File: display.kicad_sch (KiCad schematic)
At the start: 16 parts, among them J10 HDMI-A_WE_685119134923, J9 JST_SM_1x10_SM10B-SURS-TF-LF-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

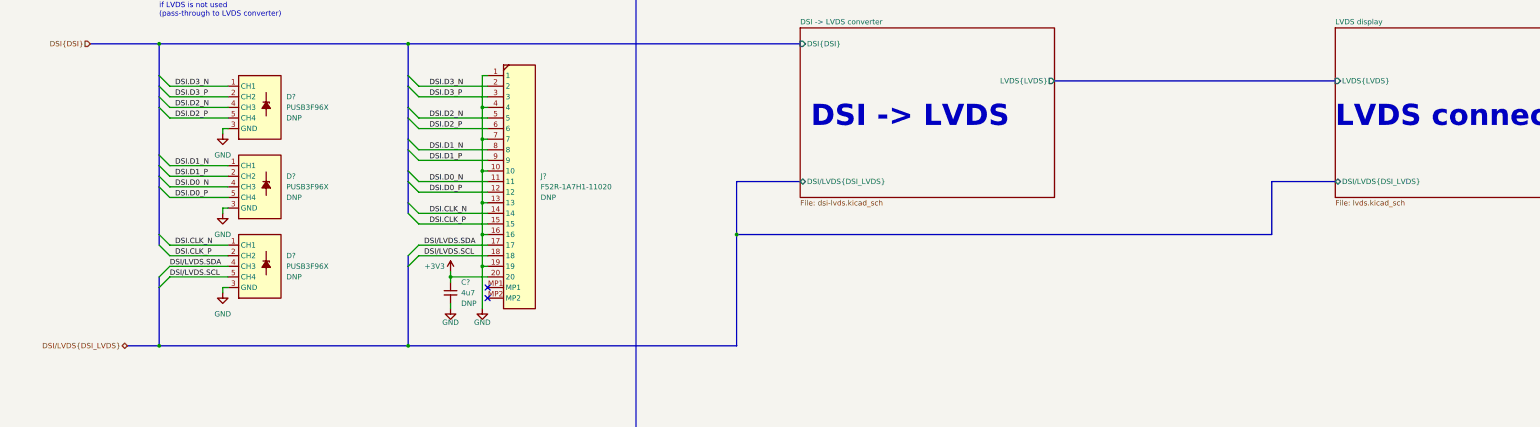
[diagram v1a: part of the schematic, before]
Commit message: [#54231] Rename bus DSI/LVDS to DisplayCtrl
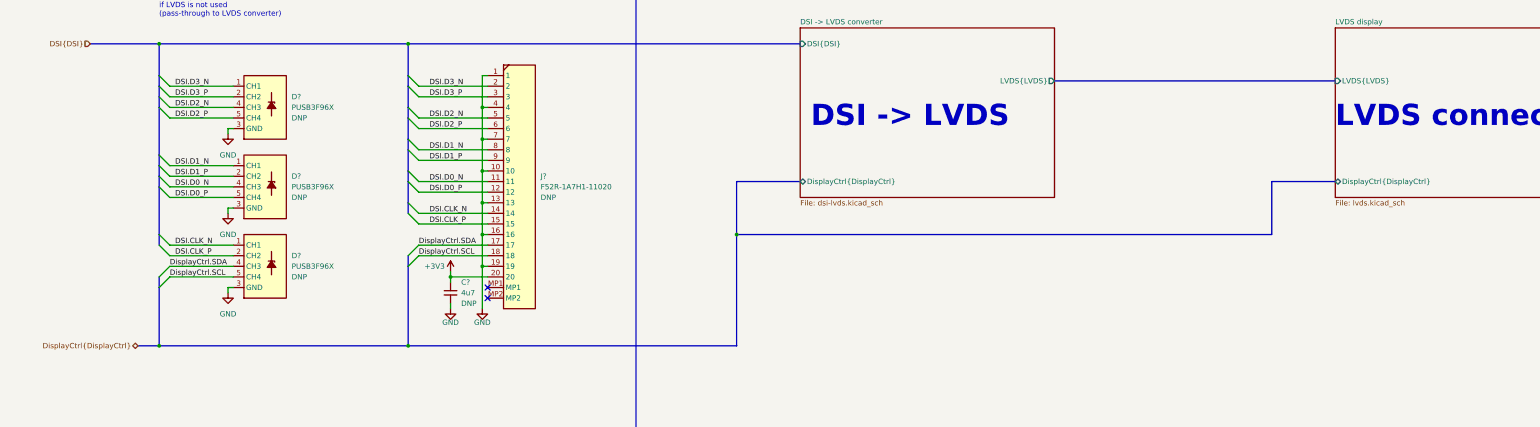
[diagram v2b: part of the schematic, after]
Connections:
- net DSI/LVDS.SCL renamed DisplayCtrl.SCL
- net DSI/LVDS.SDA renamed DisplayCtrl.SDA
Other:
- sheet DSI -> LVDS converter ports: added DisplayCtrl{DisplayCtrl}; removed DSI/LVDS{DSI_LVDS}
- sheet LVDS display ports: added DisplayCtrl{DisplayCtrl}; removed DSI/LVDS{DSI_LVDS}
- moved on the sheet: D?

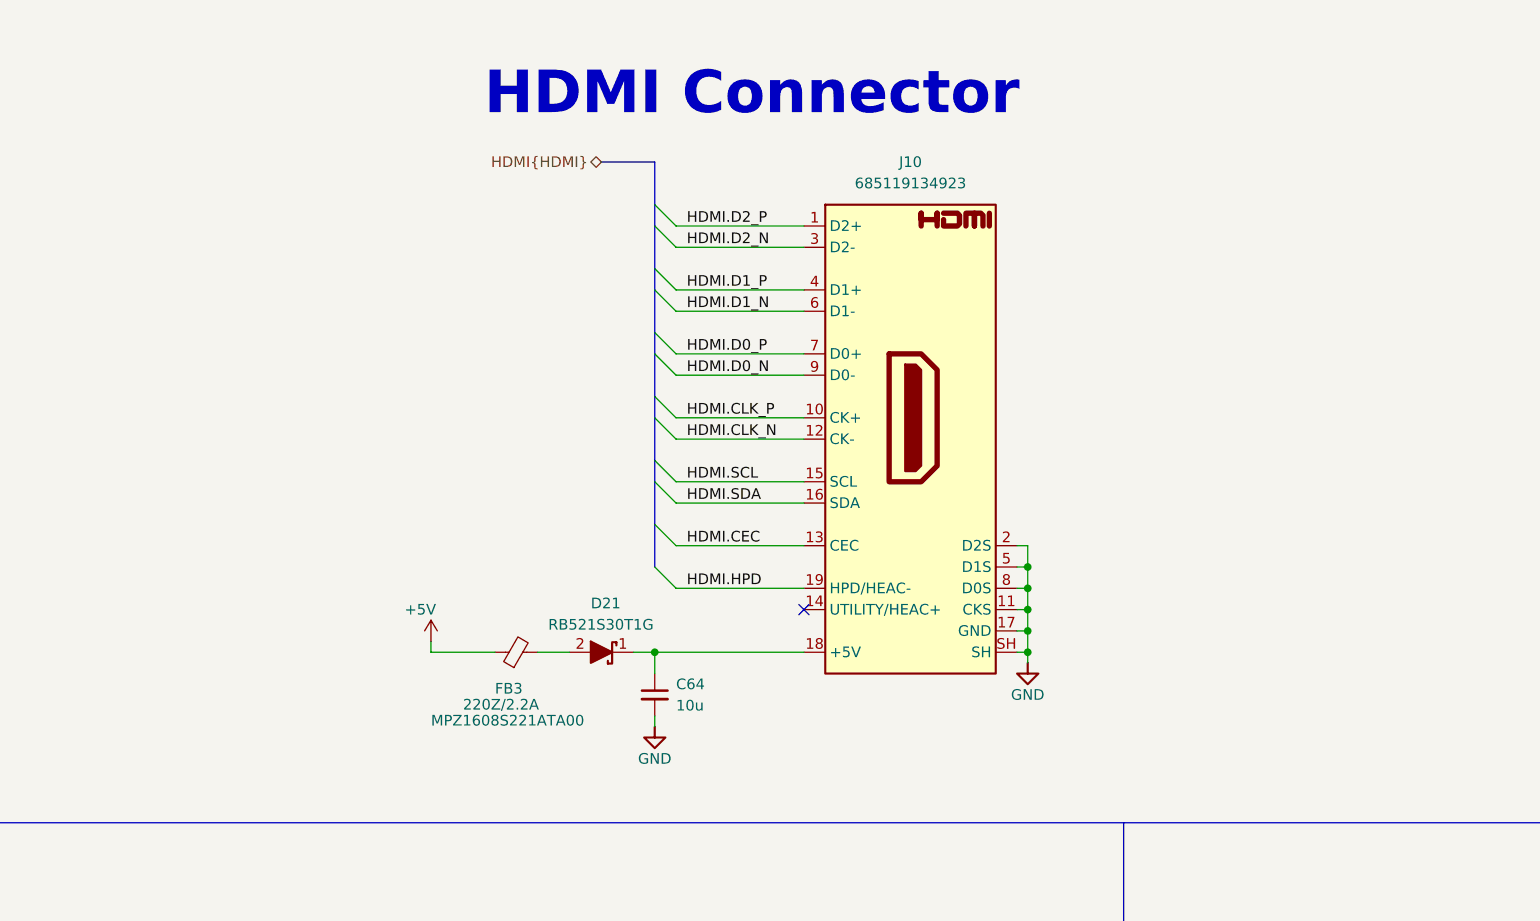
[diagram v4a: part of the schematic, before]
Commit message: [#54617] Add ESD/EMI protection on HDMI
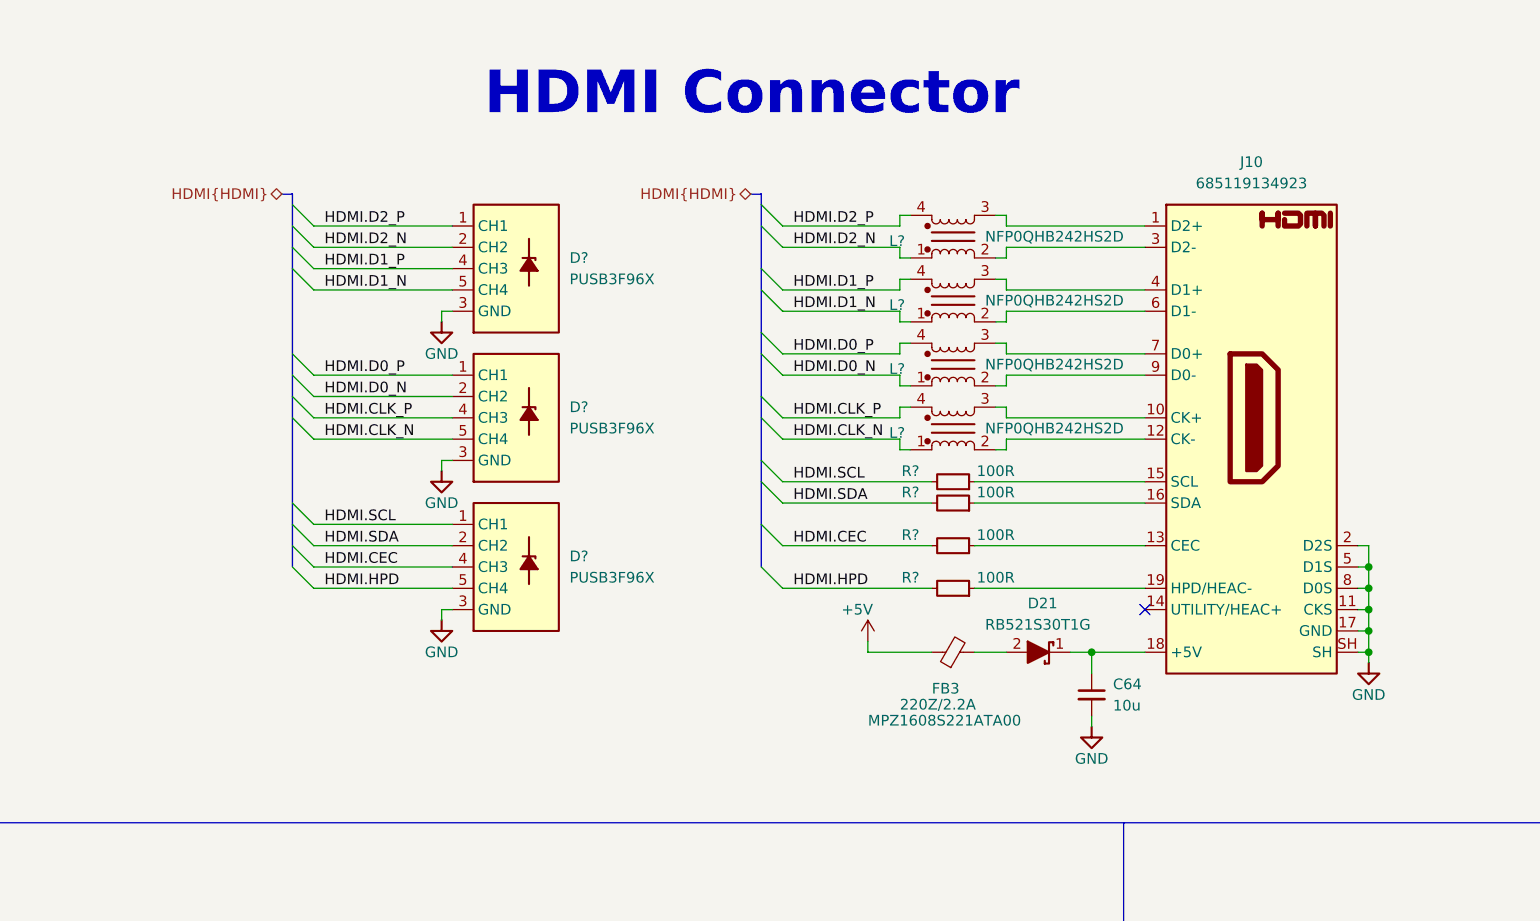
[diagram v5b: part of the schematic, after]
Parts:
- added D? (x3): PUSB3F96X_PASS, antmicro-footprints:Nexperia_DFN-10_2.5x1mm_P0.5mm, symbol antmicroTVSDiodes:PUSB3F96X_PASS
- added L? (x4): NFP0QHB242HS2D, antmicro-footprints:Choke_025020_0605Metric, symbol antmicroCommonModeChokes:Choke_NFP0QHB242HS2D
- added R? (x4): R_100R_0402, antmicro-footprints:R_0402_1005Metric, symbol antmicroResistors0402:R_100R_0402
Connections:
- net GND: now also D?.3 (GND), D?.3 (GND), D?.3 (GND), D?.8 (GND), D?.8 (GND), D?.8 (GND)
- net HDMI.CEC: now also D?.4 (CH3), D?.7 (CH3), R?.2; no longer J10.13 (CEC)
- net HDMI.CLK_N: now also D?.5 (CH4), D?.6 (CH4), L?.1; no longer J10.12 (CK-)
- net HDMI.CLK_P: now also D?.4 (CH3), D?.7 (CH3), L?.4; no longer J10.10 (CK+)
- net HDMI.D0_N: now also D?.2 (CH2), D?.9 (CH2), L?.1; no longer J10.9 (D0-)
- net HDMI.D0_P: now also D?.1 (CH1), D?.10 (CH1), L?.4; no longer J10.7 (D0+)
- net HDMI.D1_N: now also D?.5 (CH4), D?.6 (CH4), L?.1; no longer J10.6 (D1-)
- net HDMI.D1_P: now also D?.4 (CH3), D?.7 (CH3), L?.4; no longer J10.4 (D1+)
- net HDMI.D2_N: now also D?.2 (CH2), D?.9 (CH2), L?.1; no longer J10.3 (D2-)
- net HDMI.D2_P: now also D?.1 (CH1), D?.10 (CH1), L?.4; no longer J10.1 (D2+)
- net HDMI.HPD: now also D?.5 (CH4), D?.6 (CH4), R?.2; no longer J10.19 (HPD/HEAC-)
- net HDMI.SCL: now also D?.1 (CH1), D?.10 (CH1), R?.2; no longer J10.15 (SCL)
- net HDMI.SDA: now also D?.2 (CH2), D?.9 (CH2), R?.2; no longer J10.16 (SDA)
- new net: J10.19 (HPD/HEAC-), R?.1
- new net: J10.9 (D0-), L?.2
- new net: J10.7 (D0+), L?.3
- new net: J10.16 (SDA), R?.1
- new net: J10.3 (D2-), L?.2
- new net: J10.1 (D2+), L?.3
- new net: J10.12 (CK-), L?.2
- new net: J10.10 (CK+), L?.3
- new net: J10.13 (CEC), R?.1
- new net: J10.15 (SCL), R?.1
- new net: J10.6 (D1-), L?.2
- new net: J10.4 (D1+), L?.3
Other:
- moved on the sheet: C64, D21, FB3, J10

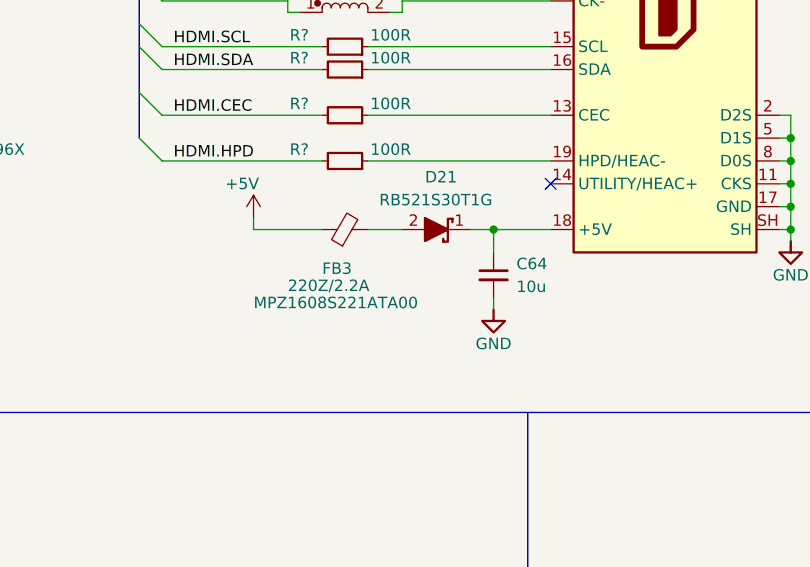
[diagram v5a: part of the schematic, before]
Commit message: [#54617] Reduce capacitors diversity
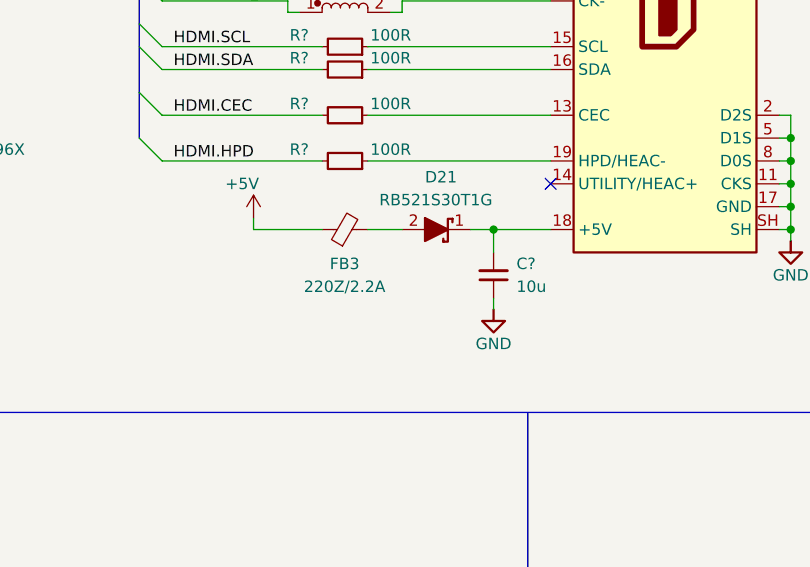
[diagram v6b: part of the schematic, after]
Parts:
- removed C64: C_10u_0603, antmicro-footprints:C_0603_1608Metric, symbol antmicroCapacitors0603:C_10u_0603
- added C?: C_10u_0402, antmicro-footprints:C_0402_1005Metric, symbol antmicroCapacitors0402:C_10u_0402
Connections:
- net GND: now also C?.1
- net at D21.1, J10.18 (+5V): now also C?.2
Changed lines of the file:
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@@
     (pin "9")
-  )
-  (symbol (lib_id "antmicroCapacitors0603:C_10u_0603") (at 152.4 90.17 90) (mirror x) (unit 1)
-    (in_bom yes) (on_board yes) (fields_autoplaced)
-    (property "Reference" "C64" (id 0) (at 154.94 91.4462 90)
-      (effects (font (size 1.27 1.27)) (justify right))
-    )
-    (property "Value" "C_10u_0603" (id 1) (at 162.56 110.49 0)
-      (effects (font (size 1.27 1.27) (thickness 0.15)) (justify left bottom) hide)
-    )
-    (property "Footprint" "antmicro-footprints:C_0603_1608Metric" (id 2) (at 165.1 110.49 0)
-      (effects (font (size 1.27 1.27) (thickness 0.15)) (justify left bottom) hide)
-    )
-    (property "Datasheet" " " (id 3) (at 167.64 110.49 0)
-      (effects (font (size 1.27 1.27) (thickness 0.15)) (justify left bottom) hide)
-    )
-    (property "Manufacturer" "Murata" (id 4) (at 172.72 110.49 0)
-      (effects (font (size 1.27 1.27) (thickness 0.15)) (justify left bottom) hide)
-    )
-    (property "MPN" "GRM188R61A106KE69D" (id 5) (at 170.18 110.49 0)
-      (effects (font (size 1.27 1.27) (thickness 0.15)) (justify left bottom) hide)
-    )
-    (property "Val" "10u" (id 6) (at 154.94 93.9862 90)
-      (effects (font (size 1.27 1.27) (thickness 0.15)) (justify right))
-    )
-    (property "License" "Apache-2.0" (id 7) (at 175.26 110.49 0)
-      (effects (font (size 1.27 1.27) (thickness 0.15)) (justify left bottom) hide)
-    )
-    (property "Author" "Antmicro" (id 8) (at 177.8 110.49 0)
-      (effects (font (size 1.27 1.27) (thickness 0.15)) (justify left bottom) hide)
-    )
-    (property "Voltage" "" (id 9) (at 180.34 110.49 0)
-      (effects (font (size 1.27 1.27)) (justify left bottom) hide)
-    )
-    (pin "1")
-    (pin "2")
   )
   (symbol (lib_id "antmicropower:GND") (at 74.93 66.04 0) (unit 1)
@@
   )
   (symbol (lib_id "antmicroFerriteBeadsandChips:FB_220Z_2.2A_TDK-MPZ_0603") (at 133.35 87.63 0) (unit 1)
-    (in_bom yes) (on_board yes)
-    (property "Reference" "FB3" (id 0) (at 133.35 92.71 0)
-      (effects (font (size 1.27 1.27)) (justify left bottom))
-    )
+    (in_bom yes) (on_board yes) (fields_autoplaced)
+    (property "Reference" "FB3" (id 0) (at 135.8519 91.44 0))
     (property "Value" "FB_220Z_2.2A_TDK-MPZ_0603" (id 1) (at 128.27 85.09 0)
       (effects (font (size 1.27 1.27) (thickness 0.15)) (justify left bottom) hide)
@@
     )
     (property "MPN" "MPZ1608S221ATA00" (id 4) (at 125.73 96.52 0)
-      (effects (font (size 1.27 1.27) (thickness 0.15)) (justify left bottom))
+      (effects (font (size 1.27 1.27) (thickness 0.15)) (justify left bottom) hide)
     )
     (property "Manufacturer" "TDK" (id 5) (at 147.32 100.33 0)
@@
       (effects (font (size 1.27 1.27) (thickness 0.15)) (justify left bottom) hide)
     )
-    (property "Val" "220Z/2.2A" (id 8) (at 129.54 94.615 0)
-      (effects (font (size 1.27 1.27)) (justify left bottom))
-    )
+    (property "Val" "220Z/2.2A" (id 8) (at 135.8519 93.98 0))
     (pin "1")
     (pin "2")
@@
     (pin "4")
   )
+  (symbol (lib_id "antmicroCapacitors0402:C_10u_0402") (at 152.4 95.25 90) (unit 1)
+    (in_bom yes) (on_board yes) (fields_autoplaced)
+    (property "Reference" "C?" (id 0) (at 154.94 91.4335 90)
+      (effects (font (size 1.27 1.27) (thickness 0.15)) (justify right))
+    )
+    (property "Value" "C_10u_0402" (id 1) (at 162.56 74.93 0)
+      (effects (font (size 1.27 1.27) (thickness 0.15)) (justify left bottom) hide)
+    )
+    (property "Footprint" "antmicro-footprints:C_0402_1005Metric" (id 2) (at 165.1 74.93 0)
+      (effects (font (size 1.27 1.27) (thickness 0.15)) (justify left bottom) hide)
+    )
+    (property "Datasheet" "https://www.yageo.com/en/Chart/Download/pdf/CC0402MRX5R5BB106" (id 3) (at 167.64 74.93 0)
+      (effects (font (size 1.27 1.27) (thickness 0.15)) (justify left bottom) hide)
+    )
+    (property "MPN" "CC0402MRX5R5BB106" (id 4) (at 170.18 74.93 0)
+      (effects (font (size 1.27 1.27) (thickness 0.15)) (justify left bottom) hide)
+    )
+    (property "Manufacturer" "YAGEO" (id 5) (at 172.72 74.93 0)
+      (effects (font (size 1.27 1.27) (thickness 0.15)) (justify left bottom) hide)
+    )
+    (property "License" "Apache-2.0" (id 6) (at 175.26 74.93 0)
+      (effects (font (size 1.27 1.27) (thickness 0.15)) (justify left bottom) hide)
+    )
+    (property "Author" "Antmicro" (id 7) (at 177.8 74.93 0)
+      (effects (font (size 1.27 1.27) (thickness 0.15)) (justify left bottom) hide)
+    )
+    (property "Val" "10u" (id 8) (at 154.94 93.9735 90)
+      (effects (font (size 1.27 1.27) (thickness 0.15)) (justify right))
+    )
+    (property "Voltage" "" (id 9) (at 180.34 74.93 0)
+      (effects (font (size 1.27 1.27)) (justify left bottom) hide)
+    )
+    (property "Dielectric" "" (id 10) (at 182.88 74.93 0)
+      (effects (font (size 1.27 1.27)) (justify left bottom) hide)
+    )
+    (pin "1")
+    (pin "2")
+  )
   (symbol (lib_id "antmicroVideoConnectors:HDMI-A_WE_685119134923") (at 158.75 36.83 0) (unit 1)

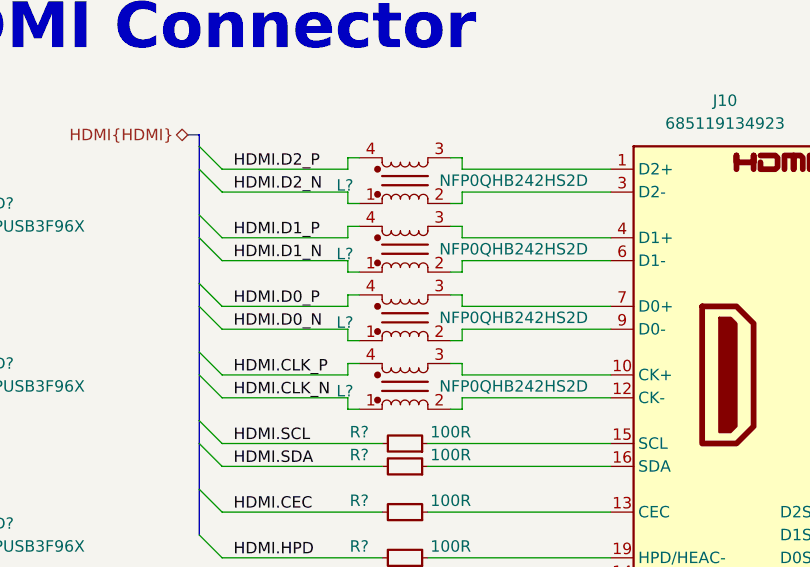
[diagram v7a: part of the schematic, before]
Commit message: [#54617] Migrate to KiCad 7
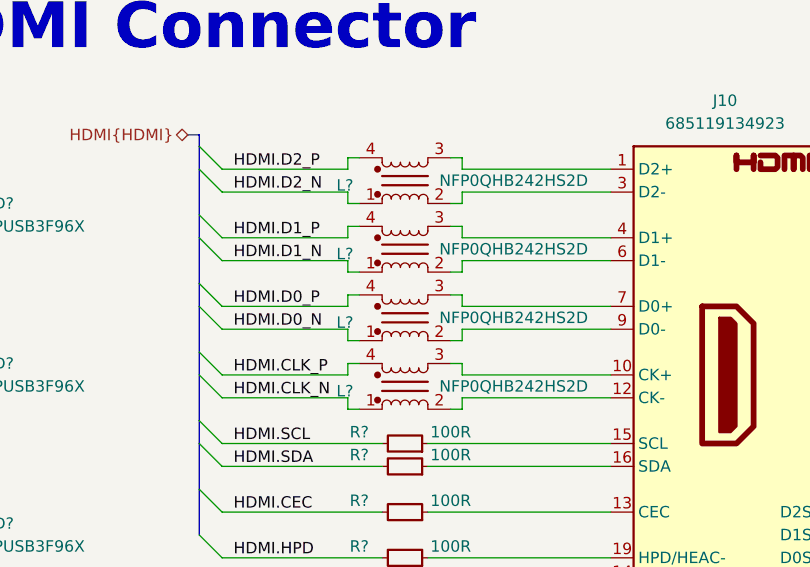
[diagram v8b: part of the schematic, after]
